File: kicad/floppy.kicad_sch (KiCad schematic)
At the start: 15 parts, among them J1 Conn_02x17_Odd_Even, J6 Floppy Power, U1 82077AA/PC8477, Y1 24 MHz

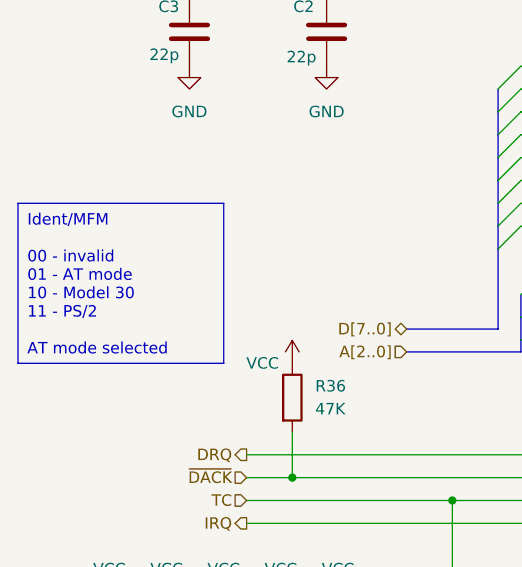
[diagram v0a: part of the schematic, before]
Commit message: hw: simplify logic, replace some SSI with GALs
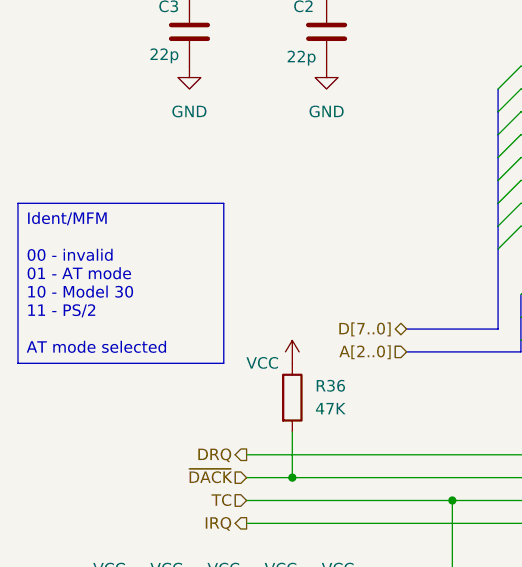
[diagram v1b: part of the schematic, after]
